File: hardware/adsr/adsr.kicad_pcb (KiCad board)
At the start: 4 copper layers, 29 x 100 mm, 63 parts, among them J1 MonoJack, J2 MonoJack, J4 Conn_02x05_Odd_Even, Q1 BC847, Q2 BC847, Q3 BC847, Q4 BC847, Q5 BC847, Q6 2N7002K, SW1 SW_DPDT_x2, SW2 SW_Push, U1 ICM7556, U2 TL074

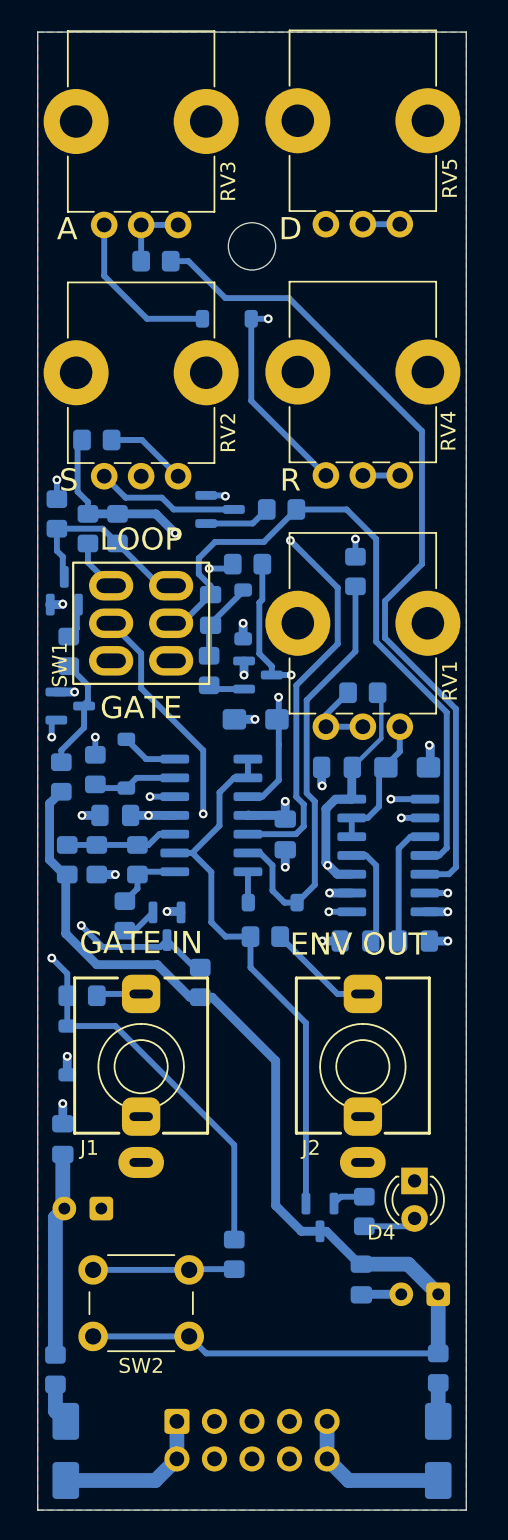
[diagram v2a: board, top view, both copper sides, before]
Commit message: Feat/external trigger (#3)
* Committing WIP on ADSR with trigger: Falstad circuit & schematic, some changes to the KiCAD schematic 
* schematic built and tested on breadboard
* added schematic screenshot from Falstad and updated the simulation circuit (link)
* routed PCB, needs cleanup
* routing cleanup
* clean up silk, check board, generate gerbers for v2
* Updated documentation for trigger input
* Updated BOM
* Updated assembly guide after assembling and testing two boards. Added annotations to schematic.
* Faceplate with art. Tested with 3DP and printouts. Adjustments marked on layout.
* Clean up and regenerate schematic.pdf (out of date before)
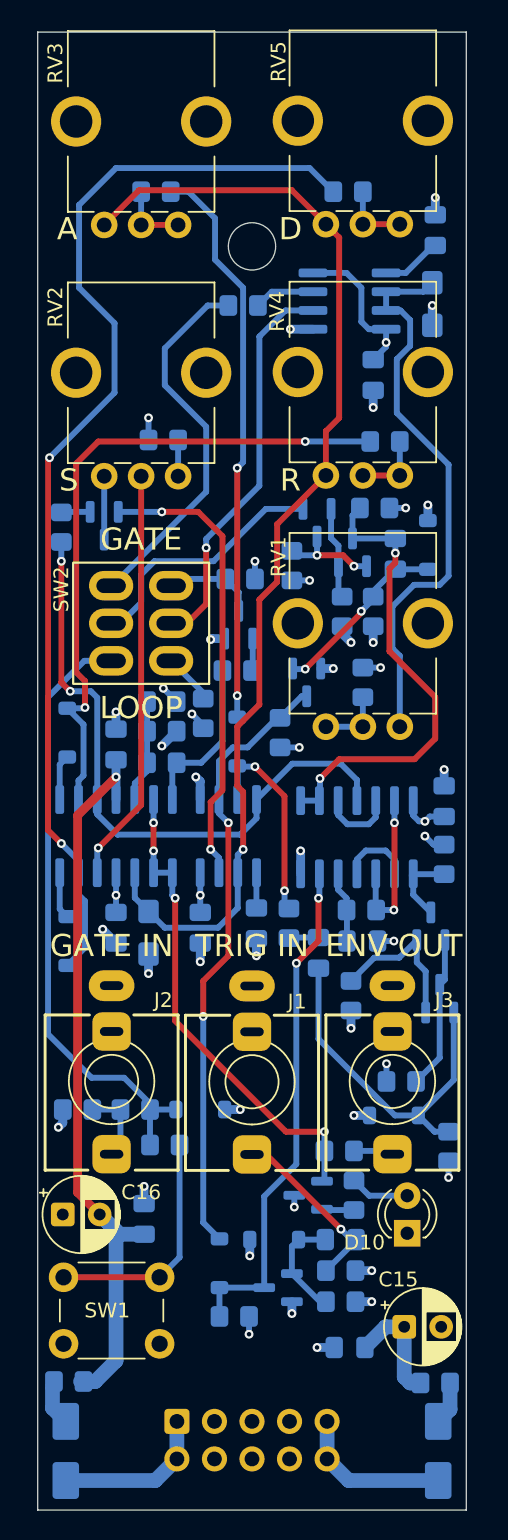
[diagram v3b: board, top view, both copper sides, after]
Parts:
- removed the D8 at (113.9, 89.4)
- removed the R27 at (101.3, 82.6)
- removed the SW1 at (107.0, 90.0)
- added C1: 10n, Capacitor_SMD:C_0805_2012Metric_Pad1.18x1.45mm_HandSolder, B.Cu at (120.5, 131.7)
- added C10: 100n, Capacitor_SMD:C_0805_2012Metric_Pad1.18x1.45mm_HandSolder, B.Cu at (111.0, 110.6)
- added C17: 100n, Capacitor_SMD:C_0805_2012Metric_Pad1.18x1.45mm_HandSolder, B.Cu at (127.5, 102.0)
- added C3: 1n, Capacitor_SMD:C_0805_2012Metric_Pad1.18x1.45mm_HandSolder, B.Cu at (122.0, 111.5)
- added C7: 10n, Capacitor_SMD:C_0805_2012Metric_Pad1.18x1.45mm_HandSolder, B.Cu at (119.0, 112.3)
- added D1: 1N4148, Diode_SMD:D_SOD-123, B.Cu at (116.0, 131.7)
- added D4: 1N4148, Diode_SMD:D_SOD-123, B.Cu at (112.3, 133.3)
- added D5: 1N4148, Diode_SMD:D_SOD-123, B.Cu at (126.4, 84.7)
- added D6: 1N4148, Diode_SMD:D_SOD-123, B.Cu at (124.1, 123.3)
- added J1: MonoJack, AudioJacks:Jack_3.5mm_QingPu_WQP-PJ301M-12_Vertical, F.Cu at (114.5, 121.0)
- added Q1: BC847, Package_TO_SOT_SMD:SOT-23, B.Cu at (116.3, 134.9)
- added Q4: BC847, Package_TO_SOT_SMD:SOT-23, B.Cu at (126.6, 110.5)
- added Q5: BC847, Package_TO_SOT_SMD:SOT-23, B.Cu at (127.2, 115.4)
- added R1: 100k, Resistor_SMD:R_0805_2012Metric_Pad1.20x1.40mm_HandSolder, B.Cu at (120.5, 133.8)
- added R10: 10k, Resistor_SMD:R_0805_2012Metric_Pad1.20x1.40mm_HandSolder, B.Cu at (121.9, 109.4)
- added R13: 22k, Resistor_SMD:R_0805_2012Metric_Pad1.20x1.40mm_HandSolder, B.Cu at (127.5, 106.0)
- added R14: 10R, Resistor_SMD:R_0805_2012Metric_Pad1.20x1.40mm_HandSolder, B.Cu at (121.2, 115.2)
- added R16: 22k, Resistor_SMD:R_0805_2012Metric_Pad1.20x1.40mm_HandSolder, B.Cu at (124.6, 121.0)
- added R19: 22k, Resistor_SMD:R_0805_2012Metric_Pad1.20x1.40mm_HandSolder, B.Cu at (127.8, 125.4)
- added R2: 100k, Resistor_SMD:R_0805_2012Metric_Pad1.20x1.40mm_HandSolder, B.Cu at (102.7, 122.9)
- added R22: 1k, Resistor_SMD:R_0805_2012Metric_Pad1.20x1.40mm_HandSolder, B.Cu at (117.0, 110.3)
- added R5: 100k, Resistor_SMD:R_0805_2012Metric_Pad1.20x1.40mm_HandSolder, B.Cu at (120.5, 135.9)
- added R7: 47k, Resistor_SMD:R_0805_2012Metric_Pad1.20x1.40mm_HandSolder, B.Cu at (113.9, 68.5)
- added R8: 47k, Resistor_SMD:R_0805_2012Metric_Pad1.20x1.40mm_HandSolder, B.Cu at (113.3, 136.9)
- added SW2: SW_DPDT_x2, Switches:SW_Dailywell_DPDT_2MD1T1B1M1, F.Cu at (107.0, 90.0)
- added U3: TLC555xD, Package_SO:SOIC-8_3.9x4.9mm_P1.27mm, B.Cu at (112.9, 104.4)
- added U4: TL074, Package_SO:SOIC-14_3.9x8.7mm_P1.27mm, B.Cu at (105.3, 104.4)
- C15: renamed from C11; moved to F.Cu
- C16: renamed from C12; moved to F.Cu
- C2: value 4U7 -> 4u7
- C8: renamed from C5; value 4U7 -> 4u7
- R11: renamed from R4; value 4k7 -> 22k
- R12: renamed from R5; value 22k -> 10R
- R15: renamed from R8; value 10k -> 22k
- R17: renamed from R28; value 10k -> 47k
- R18: renamed from R12; value 4k7 -> 22k
- R20: renamed from R6; value 10k -> 47k
- R3: renamed from R1; value 10k -> 100k
- R4: renamed from R26; value 10k -> 47k
- R9: renamed from R2; value 4k7 -> 47k
- RV1, RV2, RV3, RV4, RV5: footprint Potentiometer_THT:Potentiometer_Bourns_PTV09A-1_Single_Vertical -> Audio_Potentiometer_THT:Potentiometer_Bourns_PTV09A-1_Single_Vertical_thin
- U1: value ICM7556 -> TLC555xD; footprint Package_SO:SOIC-14_3.9x8.7mm_P1.27mm -> Package_SO:SOIC-8_3.9x4.9mm_P1.27mm
- U2: value TL074 -> HEF4093B
- moved C4 48.4 mm to (126.9, 63.4), turned to -90 degrees
- moved U1 37.6 mm to (121.1, 68.2), turned to 0 degrees
- moved C2 31.4 mm to (126.7, 68.4), turned to -90 degrees
- moved R29 29.6 mm to (123.5, 77.7), turned to 0 degrees
- moved D9 28.6 mm to (113.5, 98.0), turned to -90 degrees
- moved R20 27.4 mm to (113.7, 87.0), turned to 180 degrees
- moved C9 26.7 mm to (122.7, 73.2), turned to 90 degrees
- moved R30 25.7 mm to (121.0, 60.8), turned to 0 degrees
- moved R9 21.2 mm to (117.2, 86.1)
- moved Q7 21.0 mm to (113.6, 90.1), turned to 90 degrees
- moved Q2 20.8 mm to (118.9, 83.2), turned to -90 degrees
- moved Q3 19.7 mm to (121.3, 85.2)
- moved R12 18.7 mm to (120.6, 89.2)
- moved R21 18.3 mm to (113.5, 93.2), turned to 180 degrees
- moved R11 17.5 mm to (122.8, 82.2), turned to 180 degrees
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- renumbered C7 to C11, C8 to C12, C9 to C13, C10 to C14, C1 to C4, C3 to C5, C4 to C6, C6 to C9, D4 to D10, D5 to D11, D6 to D12, D7 to D2, D3 to D7, D2 to D8, D1 to D9, J1 to J2, J2 to J3, Q1 to Q2, Q2 to Q3, Q4 to Q6, Q3 to Q7, Q6 to Q8, Q5 to Q9, R7 to R21, R9 to R23, R17 to R24, R10 to R25, R11 to R26, R13 to R27, R14 to R28, R15 to R29, R16 to R30, R22 to R31, R21 to R32, R24 to R33, R25 to R34, R3 to R6, SW2 to SW1
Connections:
- C2 pad 1: Net-(U1B-DIS) -> Net-(U1-DIS)
- C4 pad 2: Net-(U1B-CV) -> Net-(U1-CV)
- C5 pad 1: Net-(D8-K) -> Net-(D5-K)
- C5 pad 2: Net-(SW1A-B) -> Net-(Q3-C)
- C6 pad 2: Net-(U1A-CV) -> Net-(U3-CV)
- C8 pad 1: Net-(D1-K) -> /THR
- D2 pad 1: Net-(D7-K) -> Net-(D2-K)
- D7 pad 1: Net-(D3-K) -> Net-(D7-K)
- D7 pad 2: Net-(D3-A) -> Net-(D7-A)
- D8 pad 1: Net-(D2-K) -> Net-(D8-K)
- D8 pad 2: Net-(D2-A) -> Net-(D8-A)
- D9 pad 1: Net-(D1-K) -> Net-(D9-K)
- D9 pad 2: Net-(D1-A) -> /QOUT
- Q2 pad 1: Net-(D7-K) -> Net-(Q2-B)
- Q2 pad 2: GND -> Net-(Q2-E)
- Q2 pad 3: Net-(Q1-C) -> Net-(Q2-C)
- Q3 pad 1: Net-(Q2-B) -> Net-(Q2-C)
- Q3 pad 2: GND -> Net-(Q2-E)
- Q3 pad 3: Net-(Q2-C) -> Net-(Q3-C)
- Q6 pad 1: Net-(Q4-B) -> Net-(D5-K)
- Q6 pad 3: Net-(Q4-C) -> /NTRIG
- Q8 pad 2: Net-(Q6-S) -> Net-(Q8-S)
- Q9 pad 1: Net-(Q5-B) -> Net-(Q9-B)
- R11 pad 2: Net-(Q2-C) -> Net-(Q3-C)
- R12 pad 1: Net-(Q2-B) -> Net-(Q2-E)
- R12 pad 2: Net-(Q1-C) -> GND
- R15 pad 1: Net-(Q4-B) -> Net-(D5-K)
- R15 pad 2: Net-(D8-K) -> GND
- R18 pad 2: Net-(Q4-C) -> /NTRIG
- R21 pad 2: Net-(R7-Pad2) -> /ENDOF
- R23 pad 1: Net-(U2C-+) -> Net-(U4D-+)
- R23 pad 2: Net-(R7-Pad2) -> /ENDOF
- R24 pad 2: Net-(SW1A-B) -> /NRESET
- R25 pad 1: Net-(U2C-+) -> Net-(U4D-+)
- R26 pad 2: Net-(U2C-+) -> Net-(U4D-+)
- R28 pad 1: Net-(U1A-Q) -> Net-(D9-K)
- R29 pad 1: Net-(D3-A) -> Net-(D7-A)
- R3 pad 2: Net-(D7-K) -> Net-(D2-K)
- R30 pad 1: Net-(D2-A) -> Net-(D8-A)
- R31 pad 1: Net-(Q5-B) -> Net-(Q9-B)
- R4 pad 1: Net-(D7-K) -> Net-(D2-K)
- R4 pad 2: Net-(R26-Pad2) -> Net-(R4-Pad2)
- R9 pad 1: Net-(Q1-C) -> Net-(Q2-C)
- RV1 pad 1: Net-(U1B-DIS) -> Net-(U1-DIS)
- RV2 pad 2: Net-(U2B-+) -> Net-(U4B-+)
- RV3 pad 3: Net-(D1-A) -> /THR
- RV4 pad 3: Net-(D1-K) -> /THR
- RV5 pad 3: Net-(D1-K) -> /THR
- SW1 pad 1: +12V -> Net-(R4-Pad2)
- SW1 pad 2: Net-(R26-Pad2) -> +12V
- U1 pad 1: Net-(Q6-S) -> GND
- U1 pad 2: Net-(D1-K) -> Net-(SW2A-B)
- U1 pad 3: Net-(U1A-CV) -> Net-(U1-Q)
- U1 pad 4: Net-(SW1A-B) -> +12V
- U1 pad 5: Net-(U1A-Q) -> Net-(U1-CV)
- U1 pad 6: Net-(Q4-C) -> Net-(U1-DIS)
- U1 pad 7: GND -> Net-(U1-DIS)
- U1 pad 8: Net-(SW1B-B) -> +12V
- U2 pad 1: Net-(Q5-B) -> Net-(Q4-C)
- U2 pad 10: Net-(U2C-+) -> Net-(U2-Pad10)
- U2 pad 11: -12V -> /NRESET
- U2 pad 12: Net-(SW1A-B) -> Net-(U2-Pad10)
- U2 pad 13: Net-(D3-A) -> Net-(R10-Pad1)
- U2 pad 14: Net-(D3-K) -> +12V
- U2 pad 2: Net-(Q5-B) -> Net-(U2-Pad2)
- U2 pad 3: Net-(D1-K) -> Net-(R10-Pad1)
- U2 pad 4: +12V -> Net-(U2-Pad2)
- U2 pad 5: Net-(U2B-+) -> Net-(C3-Pad1)
- U2 pad 6: Net-(D2-A) -> Net-(D4-K)
- U2 pad 7: Net-(D2-K) -> GND
- U2 pad 8: Net-(R7-Pad2) -> Net-(Q3-C)
- U2 pad 9: Net-(Q5-B) -> Net-(Q3-C)
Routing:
- net +12V: track 172.4 -> 43.8 mm, vias 4 -> 18
- net /THR: track 0.00 -> 76.8 mm, vias 0 -> 1
- net Net-(D8-A): track 0.00 -> 74.7 mm, vias 0 -> 2
- net Net-(SW1A-B): track 59.5 -> 0.00 mm, vias 1 -> 0
- net Net-(D7-K): track 61.1 -> 3.09 mm, vias 3 -> 0
- net Net-(U1A-Q): track 56.6 -> 0.00 mm
- net Net-(D1-K): track 63.7 -> 7.39 mm, vias 3 -> 0
- net Net-(D7-A): track 0.00 -> 45.3 mm, vias 0 -> 2
- net /NRESET: track 0.00 -> 43.0 mm, vias 0 -> 2
- net /NTRIG: track 0.00 -> 41.5 mm, vias 0 -> 2
- net Net-(D2-K): track 2.10 -> 41.5 mm
- net Net-(U2B-+): track 39.1 -> 0.00 mm, vias 1 -> 0
- net Net-(U1-DIS): track 0.00 -> 38.7 mm
- net Net-(R29-Pad2): track 43.4 -> 4.80 mm, vias 1 -> 0
- net Net-(D9-K): track 0.00 -> 38.4 mm, vias 0 -> 2
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- added copper zone on In1.Cu, net +12V
- removed copper zone on F.Cu, net GND
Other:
- board text added: "TRIG IN"
- board text added: "v2.0.20251123 idyllm CC BY-SA 4.0"
- board text removed: "v1.0.20250922 idyllm CC BY-SA 4.0"
